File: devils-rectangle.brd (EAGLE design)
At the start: 54 x 54 mm, 26 parts, among them J3 CORTEX_DEBUG_PTH, J6 USB-MICROB, U1 ATSAMD21G-M, U2 MIC5501-3.0YM5-TR, U3 TPD2S017, Y1 32.768KHZ

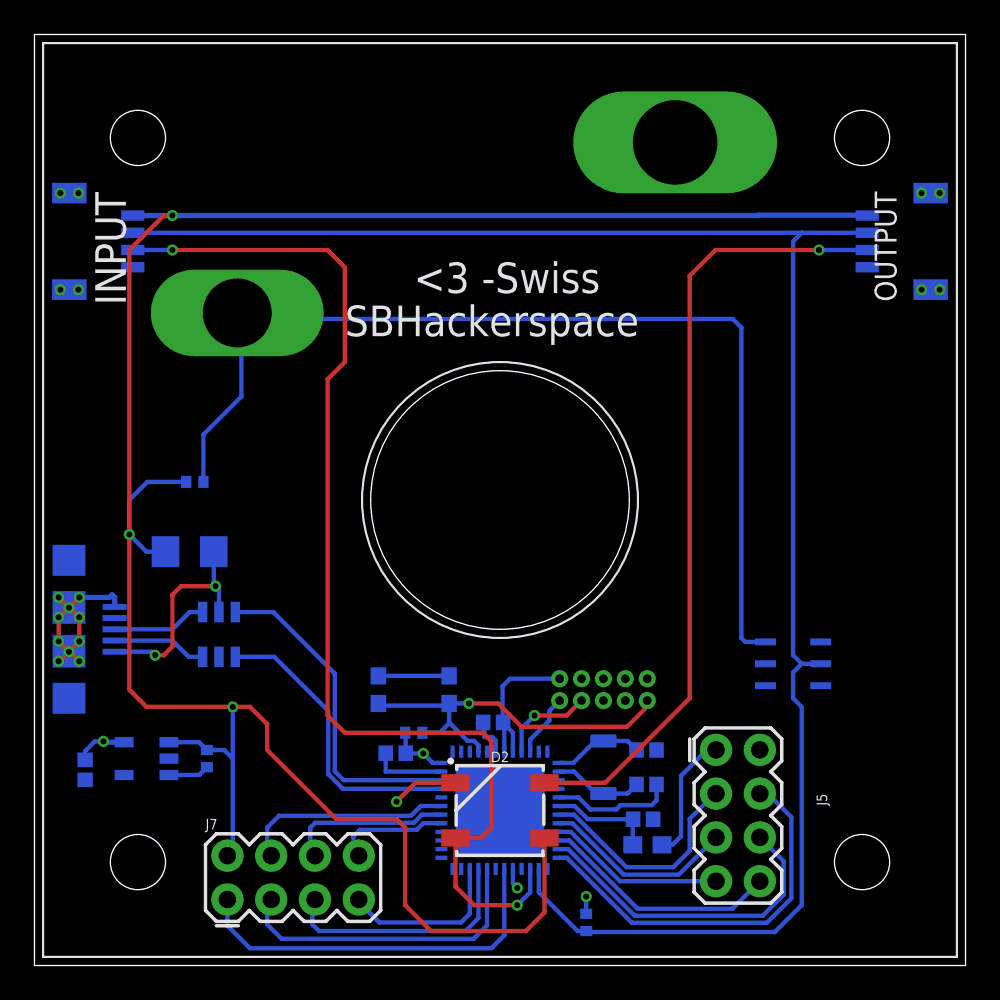
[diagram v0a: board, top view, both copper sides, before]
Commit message: updated gitignore and renamed project `
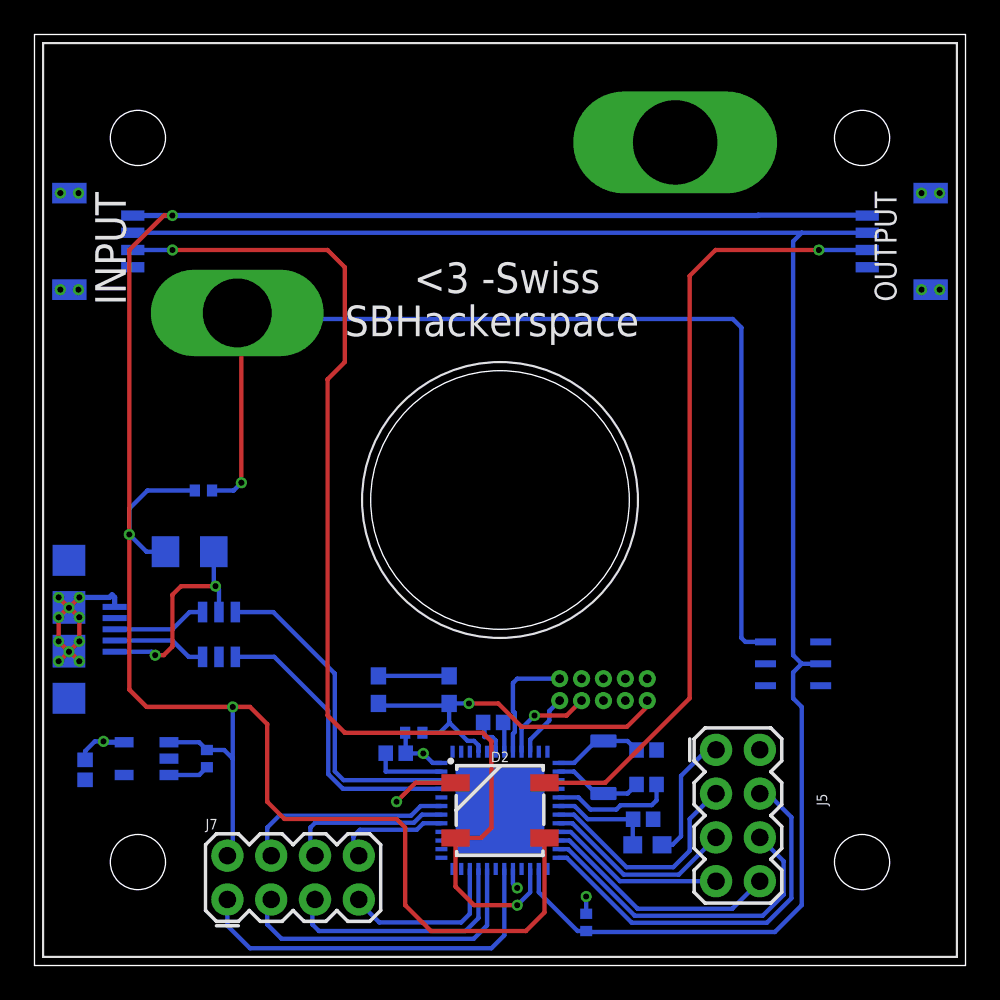
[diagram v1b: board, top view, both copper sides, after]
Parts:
- moved R4 0.71 mm to (9.80, 27.6)
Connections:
- new net N$14: C1.1, U1.43
- net VCC: no longer C1.1, U1.43
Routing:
- net VCC: track 25.5 -> 23.2 mm
- net 5V: track 130.7 -> 132.5 mm
- net N$14: track 0.00 -> 1.73 mm
- net N$10: track 59.9 -> 61.3 mm, vias 0 -> 1
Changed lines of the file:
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@@
 </element>
 <element name="C1" library="SparkFun-Capacitors" library_urn="urn:adsk.eagle:library:510" package="0402" package3d_urn="urn:adsk.eagle:package:37413/1" value="0.1uF" x="26.6" y="14.1" smashed="yes" rot="MR0">
-<attribute name="NAME" x="28.489" y="14.862" size="0.8128" layer="26" rot="MR0"/>
+<attribute name="NAME" x="27.989" y="14.862" size="0.6096" layer="26" rot="MR0"/>
 <attribute name="PROD_ID" value="CAP-12416" x="26.6" y="14.1" size="1.778" layer="28" rot="MR0" display="off"/>
 <attribute name="VALUE" value="0.1uF" x="27.389" y="15.868" size="0.6096" layer="26" rot="MR0"/>
@@
 </element>
 <element name="C3" library="SparkFun-Capacitors" library_urn="urn:adsk.eagle:library:510" package="0402" package3d_urn="urn:adsk.eagle:package:37413/1" value=".1uF" x="35.3" y="8.485" smashed="yes" rot="MR180">
-<attribute name="NAME" x="32.411" y="8.223" size="0.8128" layer="26" rot="MR180"/>
+<attribute name="NAME" x="32.911" y="8.223" size="0.6096" layer="26" rot="MR180"/>
 <attribute name="PROD_ID" value="CAP-12416" x="35.3" y="8.485" size="1.778" layer="28" rot="MR180" display="off"/>
-<attribute name="VALUE" value="0.1uF" x="30.961" y="9.217" size="0.8128" layer="26" rot="MR180"/>
+<attribute name="VALUE" value="0.1uF" x="31.961" y="9.217" size="0.6096" layer="26" rot="MR180"/>
 </element>
 <element name="C6" library="SparkFun-Capacitors" library_urn="urn:adsk.eagle:library:510" package="0402" package3d_urn="urn:adsk.eagle:package:37413/1" value="0.1uF" x="20.95" y="12.315" smashed="yes" rot="MR0">
@@
 <attribute name="VALUE" x="8.16" y="19.2" size="0.6096" layer="28" font="vector" ratio="20" rot="MR90" align="bottom-center"/>
 </element>
-<element name="R4" library="rcl" library_urn="urn:adsk.eagle:library:334" package="R0402" package3d_urn="urn:adsk.eagle:package:23547/2" value="10k" x="9.3" y="28.05" smashed="yes" rot="MR180">
-<attribute name="NAME" x="11.665" y="28.415" size="1.27" layer="26" rot="MR180"/>
-<attribute name="SPICEPREFIX" value="R" x="9.3" y="28.05" size="0.8128" layer="28" rot="MR180" display="off"/>
-<attribute name="VALUE" x="11.165" y="26.955" size="1.27" layer="28" rot="MR180"/>
+<element name="R4" library="rcl" library_urn="urn:adsk.eagle:library:334" package="R0402" package3d_urn="urn:adsk.eagle:package:23547/2" value="10k" x="9.8" y="27.55" smashed="yes" rot="MR180">
+<attribute name="NAME" x="10.165" y="28.915" size="0.6096" layer="26" rot="MR180"/>
+<attribute name="SPICEPREFIX" value="R" x="9.8" y="27.55" size="0.8128" layer="28" rot="MR180" display="off"/>
+<attribute name="VALUE" x="10.165" y="26.955" size="0.6096" layer="28" rot="MR180"/>
 </element>
 <element name="Y1" library="Seeed-Crystal Oscillator" library_urn="urn:adsk.eagle:library:466" package="X2-SMD-3.2X1.5X0.55MM" package3d_urn="urn:adsk.eagle:package:32493/1" value="32.768KHZ" x="33" y="11.5" smashed="yes" rot="MR90">
@@
 <contactref element="U1" pad="44"/>
 <contactref element="C2" pad="1"/>
-<contactref element="U1" pad="43"/>
-<contactref element="C1" pad="1"/>
 <contactref element="U2" pad="5"/>
 <via x="4" y="13" extent="1-16" drill="0.35"/>
@@
 <wire x1="4" y1="13" x2="4.05" y2="12.95" width="0.3048" layer="16"/>
 <contactref element="J5" pad="1"/>
-<wire x1="27.25" y1="12.4" x2="27.25" y2="14" width="0.254" layer="16"/>
-<wire x1="27.25" y1="14" x2="27.25" y2="14.03" width="0.254" layer="16"/>
-<wire x1="27.25" y1="14.03" x2="27.18" y2="14.1" width="0.254" layer="16"/>
-<wire x1="27.75" y1="12.4" x2="27.75" y2="13.5" width="0.254" layer="16"/>
-<wire x1="27.75" y1="13.5" x2="27.25" y2="14" width="0.254" layer="16"/>
-<wire x1="30.46" y1="16.635" x2="27.585" y2="16.635" width="0.254" layer="16"/>
-<wire x1="27.585" y1="16.635" x2="27.15" y2="16.2" width="0.254" layer="16"/>
-<wire x1="27.15" y1="16.2" x2="27.15" y2="14.13" width="0.254" layer="16"/>
-<wire x1="27.15" y1="14.13" x2="27.18" y2="14.1" width="0.254" layer="16"/>
+<wire x1="30.46" y1="16.635" x2="28" y2="16.635" width="0.254" layer="16"/>
 <wire x1="4" y1="13" x2="3.5" y2="13" width="0.254" layer="16"/>
 <wire x1="2.935" y1="12.435" x2="2.935" y2="11.93" width="0.254" layer="16"/>
@@
 <wire x1="37.5" y1="11" x2="37.5" y2="7.5" width="0.254" layer="16"/>
 <wire x1="37" y1="7" x2="36.4" y2="7" width="0.254" layer="16"/>
+<wire x1="27.75" y1="16.385" x2="28" y2="16.635" width="0.254" layer="16"/>
+<wire x1="27.75" y1="12.4" x2="27.75" y2="13.4357875" width="0.254" layer="16"/>
+<wire x1="27.75" y1="13.4357875" x2="27.859" y2="13.5447875" width="0.254" layer="16"/>
+<wire x1="27.859" y1="13.5447875" x2="27.859" y2="14.6552125" width="0.254" layer="16"/>
+<wire x1="27.859" y1="14.6552125" x2="27.75" y2="14.7642125" width="0.254" layer="16"/>
+<wire x1="27.75" y1="14.7642125" x2="27.75" y2="16.385" width="0.254" layer="16"/>
 </signal>
 <signal name="N$4">
@@
 <wire x1="21.5" y1="3.5" x2="21.5" y2="8" width="0.254" layer="1"/>
 <wire x1="21.5" y1="8" x2="21" y2="8.5" width="0.254" layer="1"/>
-<wire x1="17.5" y1="8.5" x2="13.5" y2="12.5" width="0.254" layer="1"/>
+<wire x1="14.5" y1="8.5" x2="13.5" y2="9.5" width="0.254" layer="1"/>
 <wire x1="23" y1="2" x2="21.5" y2="3.5" width="0.254" layer="1"/>
-<wire x1="21" y1="8.5" x2="17.5" y2="8.5" width="0.254" layer="1"/>
+<wire x1="21" y1="8.5" x2="14.5" y2="8.5" width="0.254" layer="1"/>
 <wire x1="5.5" y1="41.5" x2="7.5" y2="43.5" width="0.254" layer="1"/>
 <wire x1="7.5" y1="43.5" x2="8" y2="43.5" width="0.254" layer="1"/>
@@
 <wire x1="6.5" y1="15" x2="11.5" y2="15" width="0.254" layer="1"/>
 <wire x1="12.5" y1="15" x2="11.5" y2="15" width="0.254" layer="1"/>
-<wire x1="13.5" y1="12.5" x2="13.5" y2="14" width="0.254" layer="1"/>
+<wire x1="13.5" y1="9.5" x2="13.5" y2="14" width="0.254" layer="1"/>
 <wire x1="13.5" y1="14" x2="12.5" y2="15" width="0.254" layer="1"/>
 <wire x1="11.5" y1="15" x2="11.5" y2="12" width="0.254" layer="16"/>
@@
 <wire x1="7.6" y1="24" x2="6.5" y2="24" width="0.254" layer="16"/>
 <wire x1="6.5" y1="24" x2="5.5" y2="25" width="0.254" layer="16"/>
-<wire x1="8.8" y1="28.05" x2="6.55" y2="28.05" width="0.254" layer="16"/>
-<wire x1="6.55" y1="28.05" x2="5.5" y2="27" width="0.254" layer="16"/>
-<wire x1="5.5" y1="27" x2="5.5" y2="25" width="0.254" layer="16"/>
+<wire x1="9.3" y1="27.55" x2="6.55" y2="27.55" width="0.254" layer="16"/>
+<wire x1="6.55" y1="27.55" x2="5.5" y2="26.5" width="0.254" layer="16"/>
+<wire x1="5.5" y1="26.5" x2="5.5" y2="25" width="0.254" layer="16"/>
 </signal>
 <signal name="N$1">
@@
 <contactref element="U$1" pad="P$1"/>
 <contactref element="R4" pad="2"/>
-<wire x1="9.8" y1="28.05" x2="9.8" y2="30.8" width="0.254" layer="16"/>
-<wire x1="9.8" y1="30.8" x2="12" y2="33" width="0.254" layer="16"/>
-<wire x1="12" y1="33" x2="12" y2="37.61" width="0.254" layer="16"/>
+<wire x1="12" y1="28" x2="11.55" y2="27.55" width="0.254" layer="16"/>
+<wire x1="10.3" y1="27.55" x2="11.55" y2="27.55" width="0.254" layer="16"/>
 <wire x1="12" y1="37.61" x2="11.76" y2="37.85" width="0.254" layer="16"/>
 <wire x1="42.3998" y1="18.77" x2="41.23" y2="18.77" width="0.254" layer="16"/>
@@
 <wire x1="11.76" y1="37.85" x2="12.11" y2="37.5" width="0.254" layer="16"/>
 <wire x1="12.11" y1="37.5" x2="40.5" y2="37.5" width="0.254" layer="16"/>
+<via x="12" y="28" extent="1-16" drill="0.35"/>
+<wire x1="12" y1="28" x2="12" y2="37.61" width="0.254" layer="1"/>
+<wire x1="12" y1="37.61" x2="11.76" y2="37.85" width="0.254" layer="1"/>
 </signal>
 <signal name="N$12">
@@
 <contactref element="Y1" pad="2"/>
 <contactref element="C4" pad="2"/>
-<wire x1="30.4" y1="11.75" x2="31.25" y2="11.75" width="0.254" layer="16"/>
-<wire x1="32.524" y1="13.024" x2="33" y2="13.024" width="0.254" layer="16"/>
-<wire x1="31.25" y1="11.75" x2="32.524" y2="13.024" width="0.254" layer="16"/>
+<wire x1="30.4" y1="11.75" x2="31.3" y2="11.75" width="0.254" layer="16"/>
+<wire x1="32.574" y1="13.024" x2="33" y2="13.024" width="0.254" layer="16"/>
+<wire x1="31.3" y1="11.75" x2="32.574" y2="13.024" width="0.254" layer="16"/>
 <wire x1="34.92" y1="12.5" x2="34.396" y2="13.024" width="0.254" layer="16"/>
 <wire x1="34.396" y1="13.024" x2="33" y2="13.024" width="0.254" layer="16"/>
 </signal>
+<signal name="N$14">
+<contactref element="U1" pad="43"/>
+<contactref element="C1" pad="1"/>
+<wire x1="27.25" y1="12.4" x2="27.25" y2="14.03" width="0.254" layer="16"/>
+<wire x1="27.25" y1="14.03" x2="27.18" y2="14.1" width="0.254" layer="16"/>
+</signal>
 </signals>

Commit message: updated bus switch
updated bus switch to i2c to resolve arduino zero issue with onewire
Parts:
- removed U$2: DS2413P, 1wire:TSOC6
- added IC1: PCA9536, PCA9536:SO8
- added R5, R6: 4.7k, rcl:R0402
- added U$3: M74VHC1GT125, MC74VHC1GT125:SOT23-5
- J1, J2: device SparkFun-Connectors:1X04_1MM_RA -> SparkFun-Connectors:1X05_1MM
- moved R2 31.5 mm to (49.0, 29.0)
- moved J1 2.40 mm to (3.30, 42.0), turned to 270 degrees
- moved J2 1.96 mm to (50.2, 41.5), turned to 90 degrees
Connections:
- removed net 1W: J1.3, J2.2, R2.1, U$2.2, U1.14
- removed net PA22: J7.4, U1.31
- new net DI: D2.4, J1.4, U$3.4
- new net N$19: R5.2, U$3.1
- new net N$20: IC1.2
- new net N$21: IC1.3
- new net N$22: IC1.5
- new net PA19: J7.8, U1.28
- new net SCL: IC1.6, J1.3, J2.3, R6.1, U1.32
- new net SDA: IC1.7, J1.2, J2.2, R2.1, U1.31
- net 5V: now also J1.5, J2.5; no longer J1.4, J2.1
- net DIO: now also U$3.2; no longer D2.4, J1.2
- net DO: now also J2.4; no longer J2.3
- net GND: now also IC1.4, J2.1, U$3.3; no longer J2.4, U$2.1, U$2.5
- net N$10: now also IC1.1; no longer U$2.6
- net PA20: now also J7.6; no longer J7.8
- net PA21: now also J7.4; no longer J7.6
- net VCC: now also IC1.8, R5.1, R6.2, U$3.5
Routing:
- net 1W: track 101.7 -> 0.00 mm
- net SDA: track 0.00 -> 77.7 mm, vias 0 -> 2
- net SCL: track 0.00 -> 74.8 mm, vias 0 -> 2
- net DIO: track 65.8 -> 15.4 mm, vias 2 -> 1
- net DI: track 0.00 -> 47.4 mm, vias 0 -> 1
- net GND: track 56.1 -> 70.4 mm, vias 11 -> 12
- net PA22: track 12.4 -> 0.00 mm
- net VCC: track 23.2 -> 30.3 mm
- net N$10: track 61.3 -> 68.2 mm
- net PA19: track 0.00 -> 5.62 mm
- net N$19: track 0.00 -> 4.72 mm
- net DO: track 45.9 -> 43.1 mm
- net 5V: track 132.5 -> 130.2 mm
- net PA20: track 6.68 -> 8.73 mm
- net PA21: track 9.66 -> 11.7 mm
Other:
- board text added: "-"

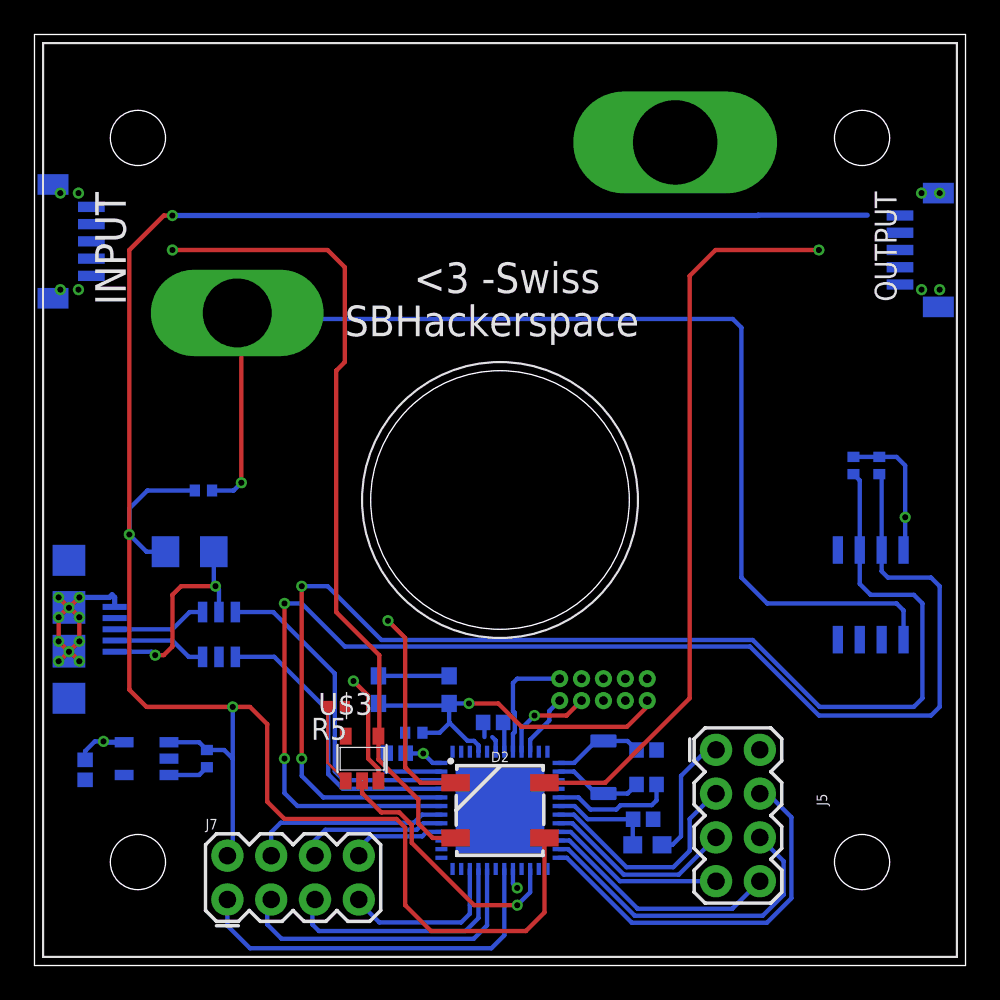
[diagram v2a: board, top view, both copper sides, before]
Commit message: replaced i2c port expander
replaced i2c port expander with an attiny85. added 3v pin to daughter board header.
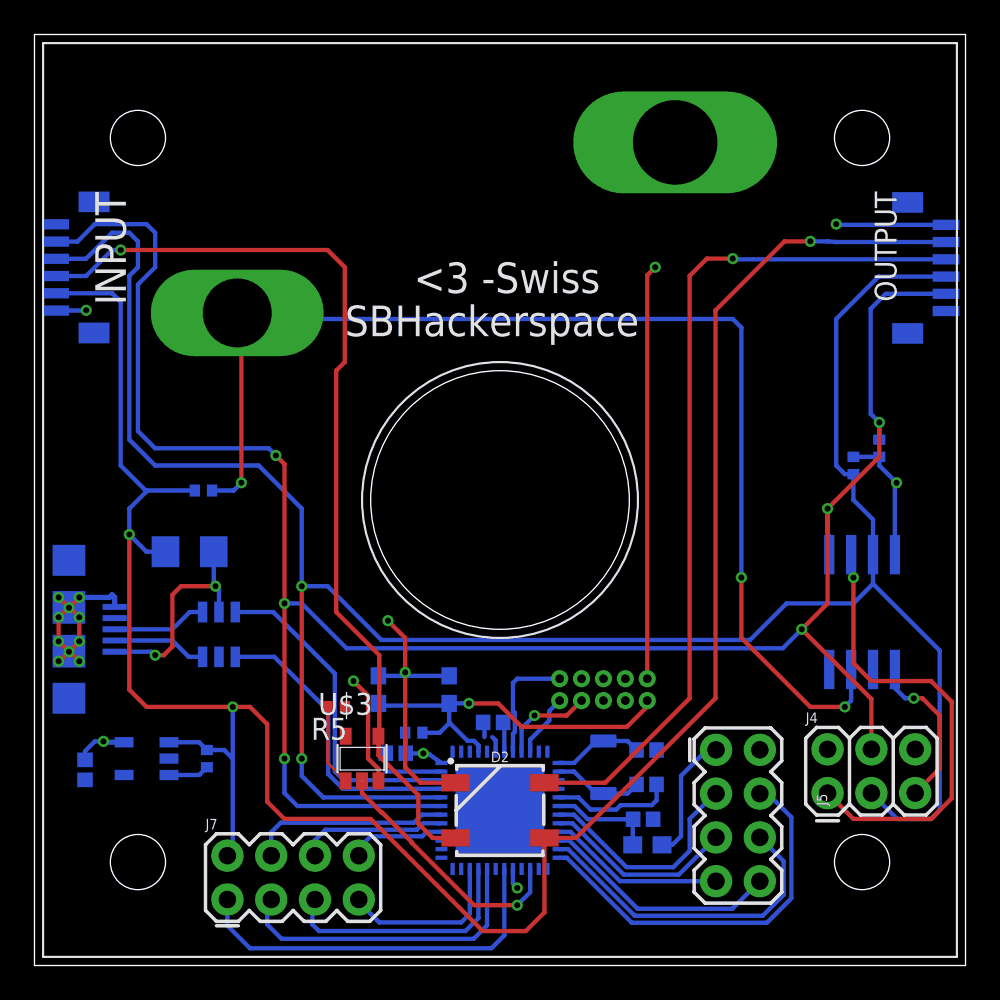
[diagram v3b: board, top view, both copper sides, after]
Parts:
- removed IC1: PCA9536, PCA9536:SO8
- added J4: (no value), SparkFun-Connectors:2X3
- added U4: ATTINY85-20S, _hhn_attiny25_45_85:SOIC8_EIAJ_208MIL
- J1, J2: device SparkFun-Connectors:1X05_1MM -> SparkFun-Connectors:1X06-1MM
- moved J1 1.74 mm to (2.50, 40.5)
- moved J2 1.72 mm to (51.6, 40.5)
- moved R2 1.00 mm to (49.0, 30.0), turned to 270 degrees
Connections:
- removed net N$20: IC1.2
- removed net N$22: IC1.5
- new net MISO: J4.1, U4.6
- new net RESET: J4.5, U4.1
- net GND: now also J4.6, U4.4; no longer IC1.4
- net N$10: now also U4.3; no longer IC1.1
- net N$21: now also U4.2; no longer IC1.3
- net SCL: now also J4.3, U4.7; no longer IC1.6
- net SDA: now also J4.4, U4.5; no longer IC1.7
- net VCC: now also J1.6, J2.6, J4.2, U4.8; no longer IC1.8
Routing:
- net SCL: track 74.8 -> 132.3 mm
- net SDA: track 77.7 -> 125.4 mm, vias 2 -> 6
- net MISO: track 0.00 -> 26.9 mm, vias 0 -> 1
- net GND: track 70.4 -> 94.5 mm, vias 12 -> 14
- net RESET: track 0.00 -> 9.42 mm, vias 0 -> 1
- net VCC: track 30.3 -> 37.9 mm, vias 4 -> 6
- net DI: track 47.4 -> 54.8 mm
- net DO: track 43.1 -> 50.3 mm
- net 5V: track 130.2 -> 133.8 mm
- net N$10: track 68.2 -> 70.7 mm, vias 1 -> 3
- net DIO: track 15.4 -> 14.8 mm
